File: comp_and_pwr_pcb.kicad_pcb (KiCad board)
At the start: 4 copper layers, 50 x 88.5 mm, 145 parts, among them IC1 TPS5430MDDAREP, IC2 ICM-42688-P, IC3 LTC4415EDHC#TRPBF, IC4 TPS259531DSGR, IC5 BMP388, IC6 W25Q32JVSSIQ, J1 USB4216-03-A, J10 Conn_01x02, J11 Conn_Coaxial, J12 Conn_Coaxial, J2 BATTERY_CONN, J3 SWD_CONN, J4 SERVO_CONN_01, J5 SERVO_CONN_02, J6 DM3AT-SF-PEJM5, J7 CAMERA_CONN_01, J8 CAMERA_CONN_02, J9 Conn_01x02, Q1 2N3904, Q10 PMV28XPEAR, Q2 BSS138, Q3 BSS138, Q4 BC847B, Q5 BC847B, Q8 PMV28XPEAR, SW1 SW_Push, SW2 SW_Push, U1 RP2040, U2 MAX-M10S, U3 MP2307DN-LF-Z, Y1 ABMM2-12.000MHZ-D1-T

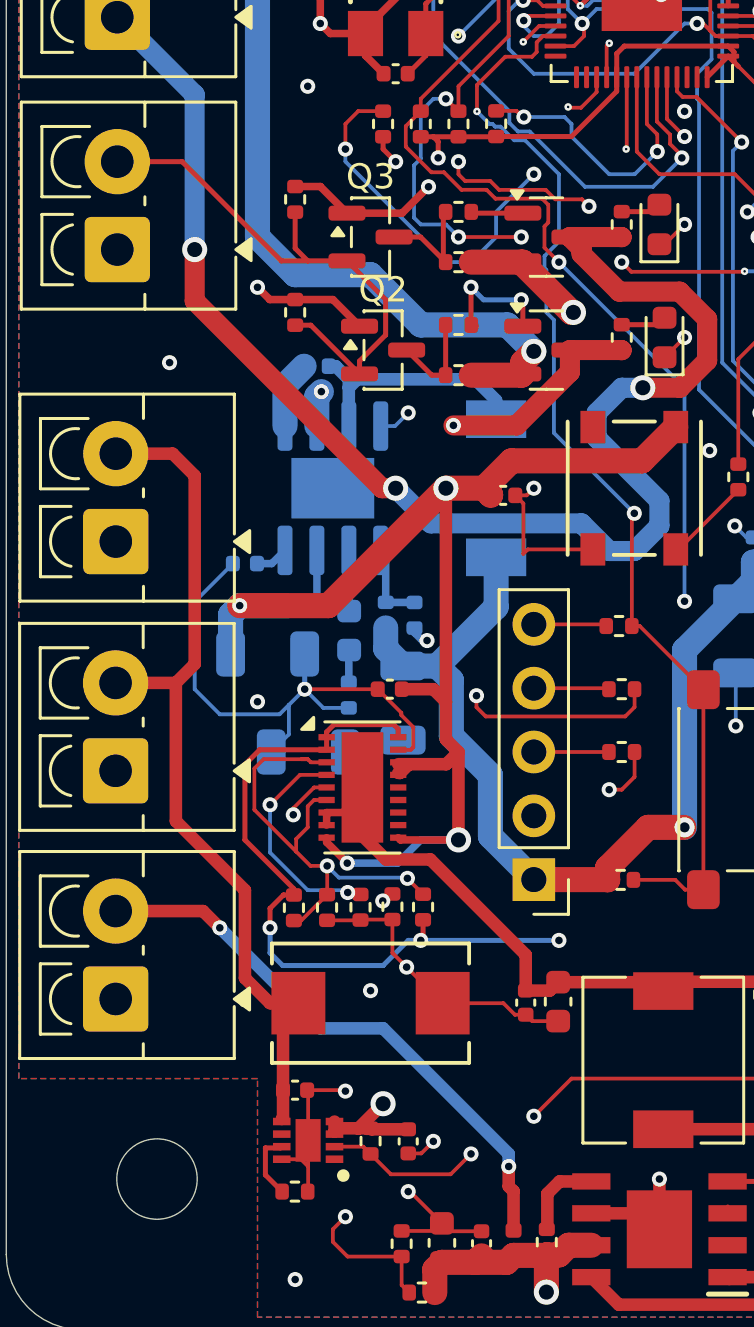
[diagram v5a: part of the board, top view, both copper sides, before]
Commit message: R28 deleted
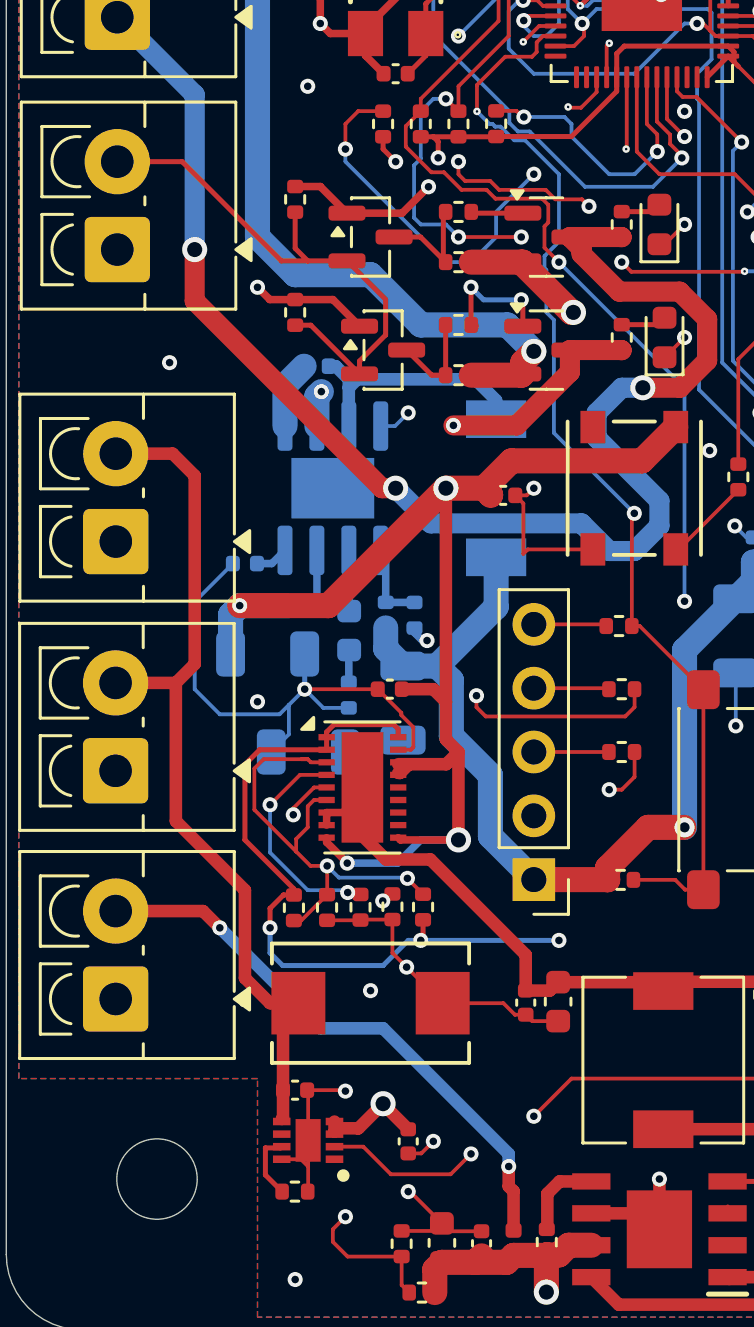
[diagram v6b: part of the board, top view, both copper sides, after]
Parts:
- removed R28: 100k, Resistor_SMD:R_0402_1005Metric
- R30: value 10K -> 10K*
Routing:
- net +5V: track 77.2 -> 76.6 mm
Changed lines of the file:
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@@
 			)
 		)
-		(property "Value" "10K"
+		(property "Value" "10K*"
 			(at 0 1.17 90)
 			(layer "F.Fab")
@@
 			(at 0 -2.4 0)
 			(layer "F.SilkS")
+			(hide yes)
 			(effects
 				(font
@@
 			(at 0 2.4 0)
 			(layer "F.Fab")
+			(hide yes)
 			(effects
 				(font
@@
 			(layer "F.Fab")
 		)
-		(fp_text user "${REFERENCE}"
-			(at 0.4375 2 90)
-			(layer "F.Fab")
-			(effects
-				(font
-					(size 0.72 0.72)
-					(thickness 0.11)
-				)
-			)
-		)
 		(pad "1" smd roundrect
 			(at -0.9375 -0.95)
@@
 		)
 	)
-	(footprint "Resistor_SMD:R_0402_1005Metric"
-		(layer "F.Cu")
-		(at 109.5 167.49 -90)
-		(descr "Resistor SMD 0402 (1005 Metric), square (rectangular) end terminal, IPC-7351 nominal, (Body size source: IPC-SM-782 page 72, https://www.pcb-3d.com/wordpress/wp-content/uploads/ipc-sm-782a_amendment_1_and_2.pdf), generated with kicad-footprint-generator")
-		(tags "resistor")
-		(property "Reference" "R28"
-			(at 0 -1.17 90)
-			(layer "F.SilkS")
-			(hide yes)
-			(effects
-				(font
-					(size 1 1)
-					(thickness 0.15)
-				)
-			)
-		)
-		(property "Value" "100k"
-			(at 0 1.17 90)
-			(layer "F.Fab")
-			(hide yes)
-			(effects
-				(font
-					(size 1 1)
-					(thickness 0.15)
-				)
-			)
-		)
-		(property "Datasheet" "~"
-			(at 0 0 90)
-			(layer "F.Fab")
-			(hide yes)
-			(effects
-				(font
-					(size 1.27 1.27)
-					(thickness 0.15)
-				)
-			)
-		)
-		(property "Description" "Resistor"
-			(at 0 0 90)
-			(layer "F.Fab")
-			(hide yes)
-			(effects
-				(font
-					(size 1.27 1.27)
-					(thickness 0.15)
-				)
-			)
-		)
-		(property ki_fp_filters "R_*")
-		(sheetname "/")
-		(sheetfile "comp_and_pwr_pcb.kicad_sch")
-		(attr smd)
-		(fp_line
-			(start -0.153641 0.38)
-			(end 0.153641 0.38)
-			(stroke
-				(width 0.12)
-				(type solid)
-			)
-			(layer "F.SilkS")
-		)
-		(fp_line
-			(start -0.153641 -0.38)
-			(end 0.153641 -0.38)
-			(stroke
-				(width 0.12)
-				(type solid)
-			)
-			(layer "F.SilkS")
-		)
-		(fp_line
-			(start -0.93 0.47)
-			(end -0.93 -0.47)
-			(stroke
-				(width 0.05)
-				(type solid)
-			)
-			(layer "F.CrtYd")
-		)
-		(fp_line
-			(start 0.93 0.47)
-			(end -0.93 0.47)
-			(stroke
-				(width 0.05)
-				(type solid)
-			)
-			(layer "F.CrtYd")
-		)
-		(fp_line
-			(start -0.93 -0.47)
-			(end 0.93 -0.47)
-			(stroke
-				(width 0.05)
-				(type solid)
-			)
-			(layer "F.CrtYd")
-		)
-		(fp_line
-			(start 0.93 -0.47)
-			(end 0.93 0.47)
-			(stroke
-				(width 0.05)
-				(type solid)
-			)
-			(layer "F.CrtYd")
-		)
-		(fp_line
-			(start -0.525 0.27)
-			(end -0.525 -0.27)
-			(stroke
-				(width 0.1)
-				(type solid)
-			)
-			(layer "F.Fab")
-		)
-		(fp_line
-			(start 0.525 0.27)
-			(end -0.525 0.27)
-			(stroke
-				(width 0.1)
-				(type solid)
-			)
-			(layer "F.Fab")
-		)
-		(fp_line
-			(start -0.525 -0.27)
-			(end 0.525 -0.27)
-			(stroke
-				(width 0.1)
-				(type solid)
-			)
-			(layer "F.Fab")
-		)
-		(fp_line
-			(start 0.525 -0.27)
-			(end 0.525 0.27)
-			(stroke
-				(width 0.1)
-				(type solid)
-			)
-			(layer "F.Fab")
-		)
-		(pad "1" smd roundrect
-			(at -0.51 0 270)
-			(size 0.54 0.64)
-			(layers "F.Cu" "F.Mask" "F.Paste")
-			(roundrect_rratio 0.25)
-			(net 5 "+5V")
-			(pintype "passive")
-		)
-		(pad "2" smd roundrect
-			(at 0.51 0 270)
-			(size 0.54 0.64)
-			(layers "F.Cu" "F.Mask" "F.Paste")
-			(roundrect_rratio 0.25)
-			(net 27 "/CAMERA_SWITCH")
-			(pintype "passive")
-		)
-		(embedded_fonts no)
-		(model "${KICAD9_3DMODEL_DIR}/Resistor_SMD.3dshapes/R_0402_1005Metric.step"
-			(offset
-				(xyz 0 0 0)
-			)
-			(scale
-				(xyz 1 1 1)
-			)
-			(rotate
-				(xyz 0 0 0)
-			)
-		)
-	)
 	(footprint "Package_TO_SOT_SMD:SOT-23"
 		(layer "F.Cu")
@@
 			(at 0 -2.4 0)
 			(layer "F.SilkS")
+			(hide yes)
 			(effects
 				(font
@@
 			(at 0 2.4 0)
 			(layer "F.Fab")
+			(hide yes)
 			(effects
 				(font
@@
 			(layer "F.Fab")
 		)
-		(fp_text user "${REFERENCE}"
-			(at 0 0 90)
-			(layer "F.Fab")
-			(effects
-				(font
-					(size 0.72 0.72)
-					(thickness 0.11)
-				)
-			)
-		)
 		(pad "1" smd roundrect
 			(at -0.9375 -0.95)
@@
 	)
 	(segment
-		(start 111 167.02)
-		(end 109.54 167.02)
-		(width 0.5)
-		(layer "F.Cu")
-		(net 5)
-	)
-	(segment
 		(start 111 152.486902)
 		(end 110.601652 152.486902)
@@
 	)
 	(segment
-		(start 109.5 166.98)
-		(end 109 166.98)
-		(width 0.5)
-		(layer "F.Cu")
-		(net 5)
-	)
-	(segment
 		(start 112.5 150)
 		(end 112 149.5)
@@
 	)
 	(segment
-		(start 109 166.98)
-		(end 108.196462 166.98)
+		(start 110 166.02)
+		(end 111 167.02)
 		(width 0.5)
 		(layer "F.Cu")
@@
 	)
 	(segment
-		(start 109.54 167.02)
-		(end 109.5 166.98)
+		(start 109 166.98)
+		(end 108.196462 166.98)
 		(width 0.5)
 		(layer "F.Cu")
@@
 	)
 	(segment
+		(start 110 166)
+		(end 110 166.02)
+		(width 0.5)
+		(layer "F.Cu")
+		(net 5)
+	)
+	(segment
 		(start 110.677652 152.834902)
 		(end 110.601652 152.834902)
@@
 	)
 	(segment
-		(start 109.5 168)
-		(end 110.31102 168.81102)
-		(width 0.15)
-		(layer "F.Cu")
-		(net 27)
-	)
-	(segment
-		(start 109.21142 167.71142)
-		(end 109.5 168)
+		(start 112.68898 168.81102)
+		(end 113.5 168)
 		(width 0.15)
 		(layer "F.Cu")
@@
 	)
 	(segment
-		(start 112.68898 168.81102)
-		(end 113.5 168)
+		(start 110.31102 168.81102)
+		(end 112.68898 168.81102)
 		(width 0.15)
 		(layer "F.Cu")
@@
 	)
 	(segment
-		(start 110.31102 168.81102)
-		(end 112.68898 168.81102)
+		(start 109.21142 167.71142)
+		(end 110.31102 168.81102)
 		(width 0.15)
 		(layer "F.Cu")

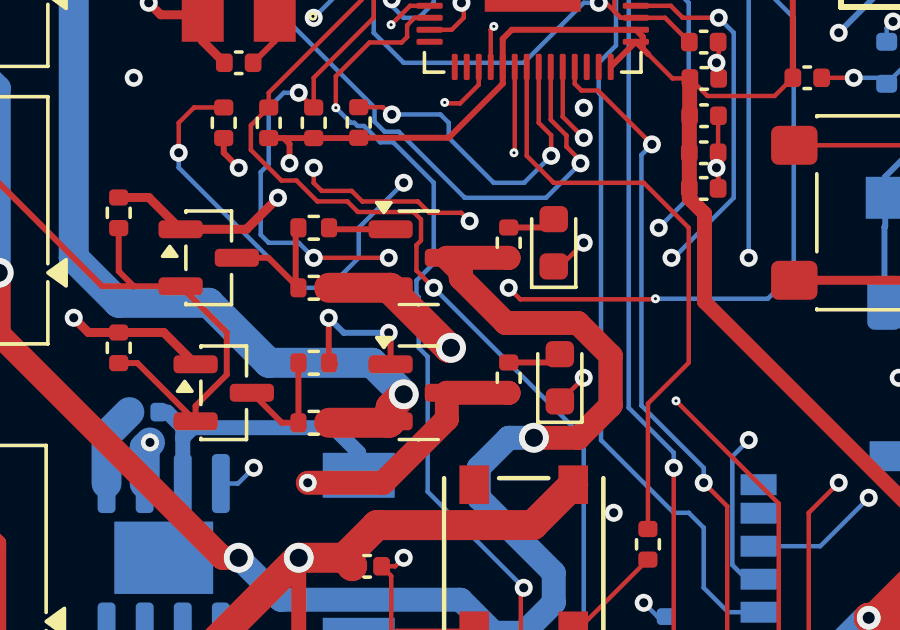
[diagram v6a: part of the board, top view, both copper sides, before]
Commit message: Pyro mosfet change
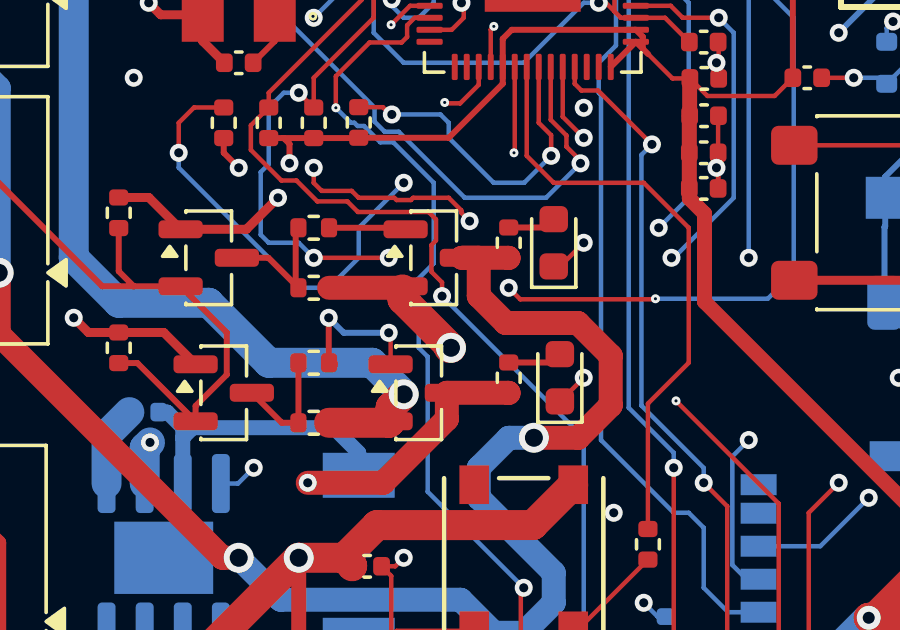
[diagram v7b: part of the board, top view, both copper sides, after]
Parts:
- removed Q10, Q8: PMV28XPEAR, Package_TO_SOT_SMD:SOT-23
- added Q6: MMBT3904, Package_TO_SOT_SMD:SOT-23, F.Cu at (117.0, 131.5)
- added Q7: MMBT3904, Package_TO_SOT_SMD:SOT-23, F.Cu at (116.5, 136.0)
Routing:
- net Net-(Q6-B): track 2.07 -> 2.64 mm

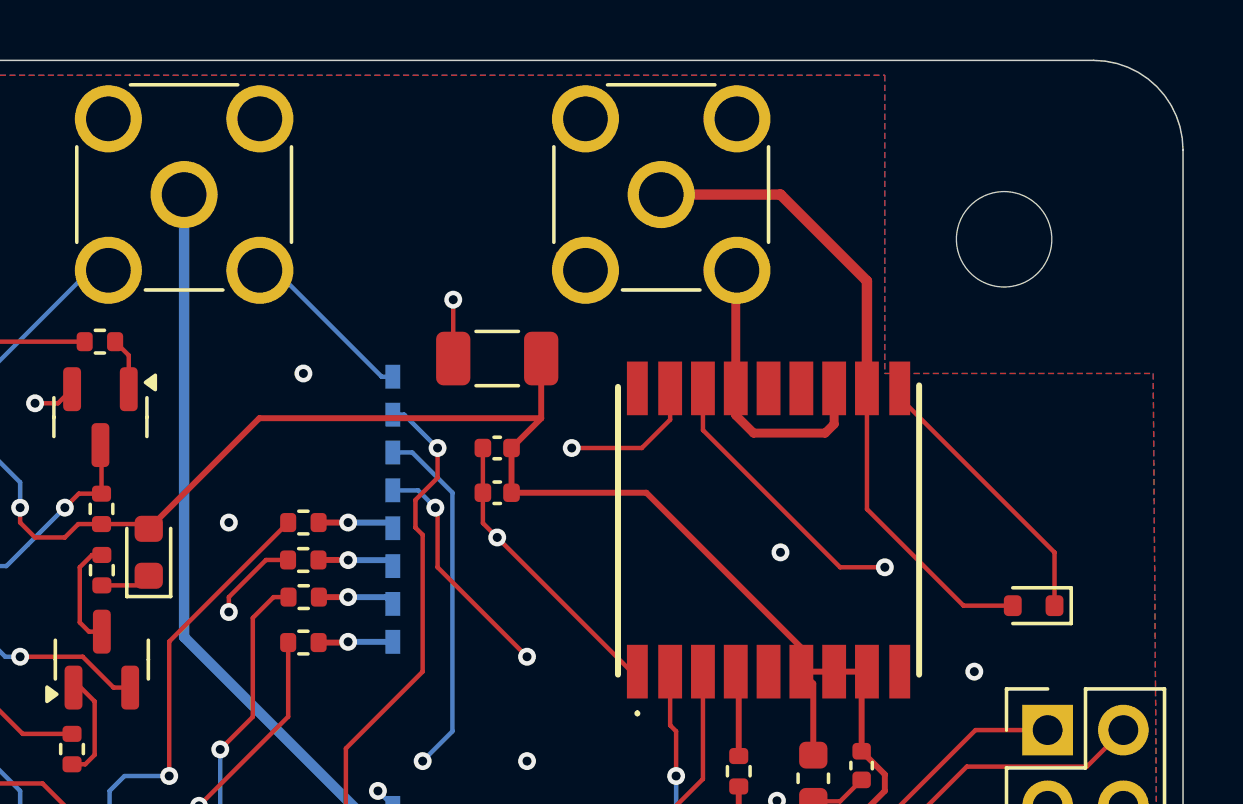
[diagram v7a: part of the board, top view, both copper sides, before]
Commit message: TVS diodes fixed
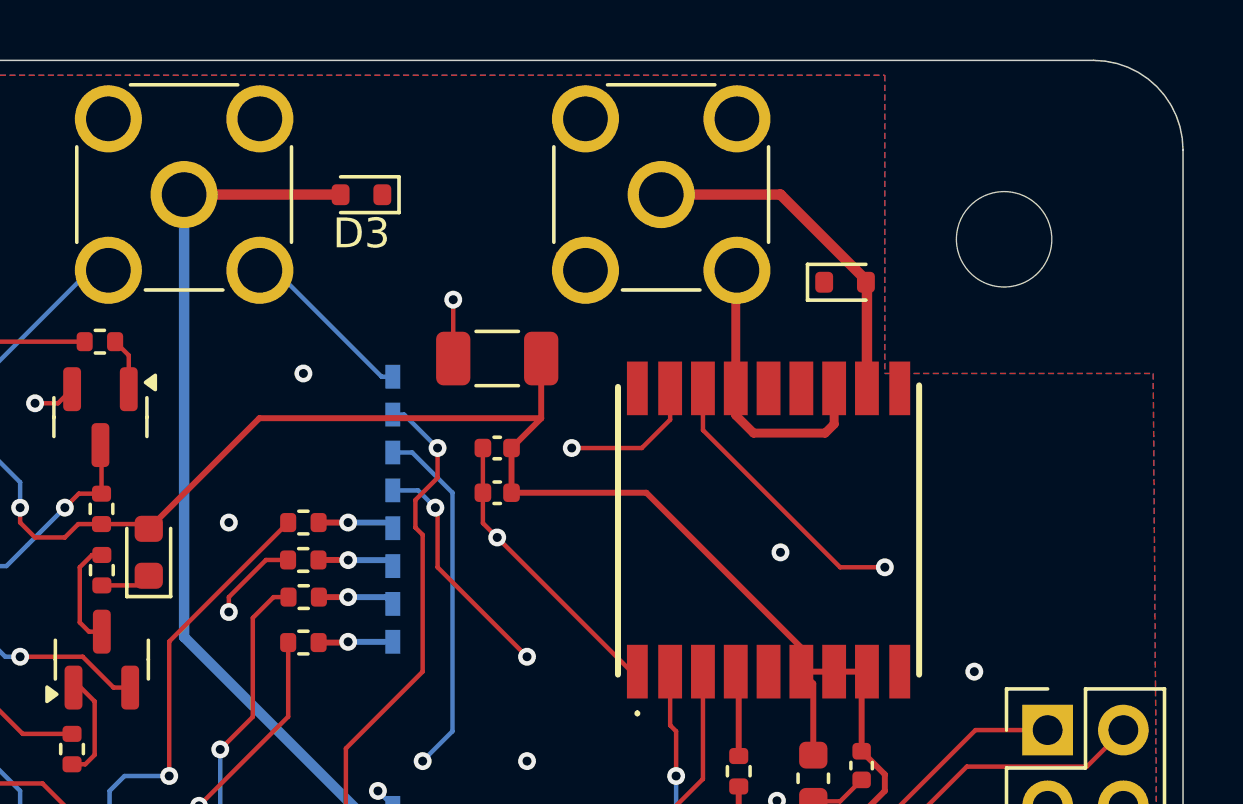
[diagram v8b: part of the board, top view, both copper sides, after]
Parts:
- added D3: D_TVS, Diode_SMD:D_SOD-523, F.Cu at (117.4, 91.0)
- moved D5 12.6 mm to (133.7, 93.9), turned to 0 degrees
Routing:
- net Net-(D5-A2): track 22.2 -> 11.7 mm
- net GND: track 276.9 -> 267.5 mm
- net Net-(D3-A2): track 24.7 -> 30.0 mm
